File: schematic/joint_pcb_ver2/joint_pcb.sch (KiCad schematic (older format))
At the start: 0 parts

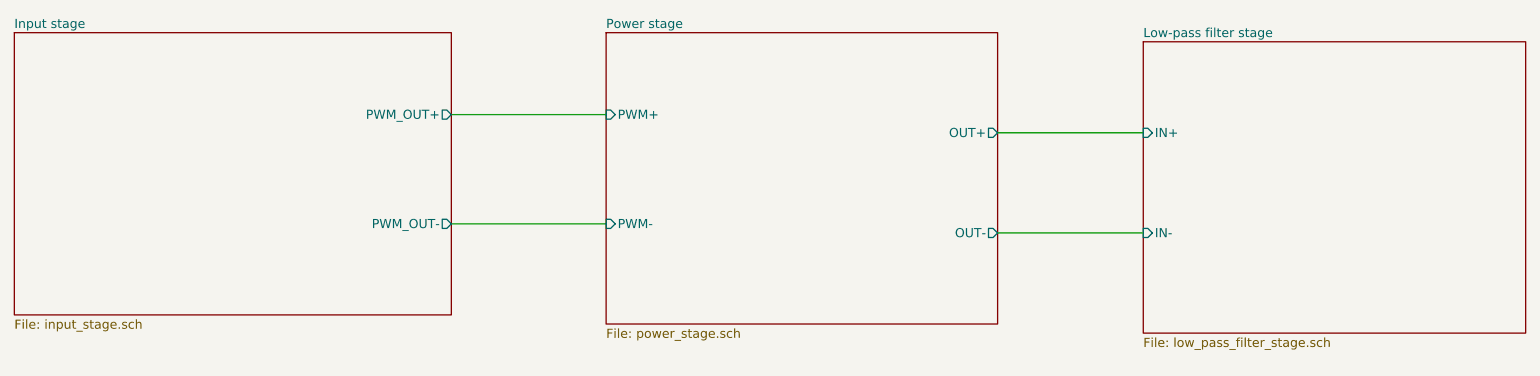
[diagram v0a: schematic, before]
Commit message: connect up 10V
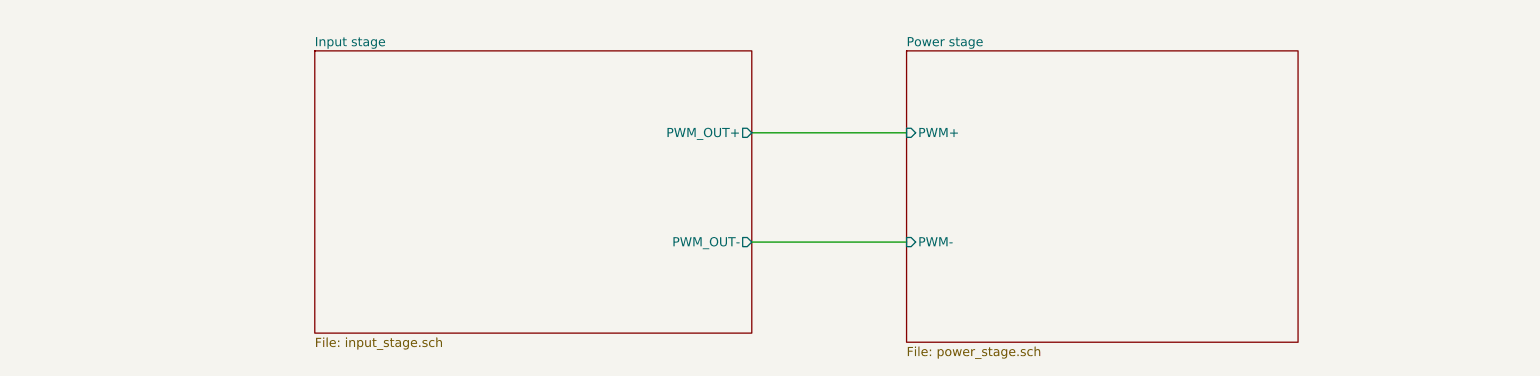
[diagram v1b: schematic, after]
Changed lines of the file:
@@
 $Descr A4 11693 8268
 encoding utf-8
-Sheet 1 4
+Sheet 1 3
 Title ""
 Date ""
@@
 $EndDescr
 $Sheet
-S 1600 3000 2400 1550
+S 3250 3100 2400 1550
 U 6131B79C
 F0 "Input stage" 50
 F1 "input_stage.sch" 50
-F2 "PWM_OUT+" O R 4000 3450 50
-F3 "PWM_OUT-" O R 4000 4050 50
+F2 "PWM_OUT+" O R 5650 3550 50
+F3 "PWM_OUT-" O R 5650 4150 50
 $EndSheet
 $Sheet
-S 4850 3000 2150 1600
+S 6500 3100 2150 1600
 U 6133C499
 F0 "Power stage" 50
 F1 "power_stage.sch" 50
-F2 "PWM+" I L 4850 3450 50
-F3 "PWM-" I L 4850 4050 50
-F4 "OUT+" O R 7000 3550 50
-F5 "OUT-" O R 7000 4100 50
-$EndSheet
-$Sheet
-S 7800 3050 2100 1600
-U 6133C589
-F0 "Low-pass filter stage" 50
-F1 "low_pass_filter_stage.sch" 50
-F2 "IN+" I L 7800 3550 50
-F3 "IN-" I L 7800 4100 50
+F2 "PWM+" I L 6500 3550 50
+F3 "PWM-" I L 6500 4150 50
 $EndSheet
 Wire Wire Line
-	7000 3550 7800 3550
+	5650 3550 6500 3550
 Wire Wire Line
-	7000 4100 7800 4100
-Wire Wire Line
-	4000 3450 4850 3450
-Wire Wire Line
-	4000 4050 4850 4050
+	5650 4150 6500 4150
 $EndSCHEMATC
